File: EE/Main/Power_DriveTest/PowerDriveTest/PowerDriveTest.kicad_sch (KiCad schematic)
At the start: 46 parts, among them J1 Conn_01x02_Male, J2 Conn_01x03_Pin, J4 Conn_01x03_Pin, J5 Conn_01x03_Pin, P1 USB_C_Plug_USB2.0, Q1 Q_PMOS_GSD, Q2 Q_NMOS_GSD, SW1 SW_SPST, U1 LM3670MF-3.3, U4 MCP73832-2-OT

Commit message: Routine Checkout
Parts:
- removed R7: 0, Resistor_SMD:R_0402_1005Metric, symbol Device:R
- removed SW1: SW_SPST, Button_Switch_SMD:SW_Tactile_SPST_NO_Straight_CK_PTS636Sx25SMTRLFS, symbol Switch:SW_SPST
- added SW2: SW_DPST, symbol Switch:SW_DPST
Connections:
- net +3V3: now also SW2.1
- net GATE_EN: now also SW2.3
- net at R9.1: now also SW2.4
- new net BTN_SNS: SW2.2
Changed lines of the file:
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@@
 	)
 	(junction
-		(at 104.14 69.85)
-		(diameter 0)
-		(color 0 0 0 0)
-	)
-	(junction
 		(at 271.78 83.82)
 		(diameter 0)
@@
 	)
 	(junction
-		(at 118.11 69.85)
-		(diameter 0)
-		(color 0 0 0 0)
-	)
-	(junction
 		(at 233.68 130.81)
 		(diameter 0)
@@
 	(wire
 		(pts
-			(xy 104.14 69.85) (xy 104.14 73.66)
-		)
-		(stroke
-			(width 0)
-			(type default)
-		)
-	)
-	(wire
-		(pts
 			(xy 242.57 73.66) (xy 242.57 76.2)
 		)
@@
 	(wire
 		(pts
-			(xy 95.25 69.85) (xy 104.14 69.85)
+			(xy 95.25 69.85) (xy 106.68 69.85)
 		)
 		(stroke
@@
 	(wire
 		(pts
-			(xy 271.78 97.79) (xy 271.78 95.25)
+			(xy 116.84 69.85) (xy 123.19 69.85)
 		)
 		(stroke
@@
 	(wire
 		(pts
-			(xy 90.932 109.22) (xy 86.36 109.22)
+			(xy 271.78 97.79) (xy 271.78 95.25)
 		)
 		(stroke
@@
 	(wire
 		(pts
-			(xy 256.286 137.414) (xy 254.254 137.414)
+			(xy 90.932 109.22) (xy 86.36 109.22)
 		)
 		(stroke
@@
 	(wire
 		(pts
-			(xy 146.05 67.31) (xy 146.05 53.34)
+			(xy 256.286 137.414) (xy 254.254 137.414)
 		)
 		(stroke
@@
 	(wire
 		(pts
-			(xy 118.11 66.04) (xy 118.11 69.85)
+			(xy 146.05 67.31) (xy 146.05 53.34)
 		)
 		(stroke
@@
 	(wire
 		(pts
-			(xy 118.11 73.66) (xy 113.03 73.66)
-		)
-		(stroke
-			(width 0)
-			(type default)
-		)
-	)
-	(wire
-		(pts
 			(xy 85.09 55.88) (xy 85.09 69.85)
 		)
@@
 	(wire
 		(pts
-			(xy 118.11 69.85) (xy 123.19 69.85)
-		)
-		(stroke
-			(width 0)
-			(type default)
-		)
-	)
-	(wire
-		(pts
 			(xy 123.19 69.85) (xy 123.19 73.66)
 		)
@@
 	(wire
 		(pts
-			(xy 104.14 73.66) (xy 105.41 73.66)
-		)
-		(stroke
-			(width 0)
-			(type default)
-		)
-	)
-	(wire
-		(pts
 			(xy 250.19 90.17) (xy 251.46 90.17)
 		)
@@
 	(wire
 		(pts
-			(xy 104.14 66.04) (xy 104.14 69.85)
-		)
-		(stroke
-			(width 0)
-			(type default)
-		)
-	)
-	(wire
-		(pts
 			(xy 256.286 135.89) (xy 256.286 137.414)
 		)
@@
 	(wire
 		(pts
-			(xy 118.11 69.85) (xy 118.11 73.66)
-		)
-		(stroke
-			(width 0)
-			(type default)
-		)
-	)
-	(wire
-		(pts
 			(xy 252.73 83.82) (xy 255.27 83.82)
 		)
@@
 		)
 	)
-	(wire
-		(pts
-			(xy 114.3 66.04) (xy 118.11 66.04)
-		)
-		(stroke
-			(width 0)
-			(type default)
-		)
-	)
 	(text "Simulate GPIO toggles"
 		(exclude_from_sim no)
@@
 		)
 	)
+	(label "BTN_SNS"
+		(at 116.84 74.93 270)
+		(fields_autoplaced yes)
+		(effects
+			(font
+				(size 1.27 1.27)
+			)
+			(justify right bottom)
+		)
+	)
 	(symbol
 		(lib_id "Device:R")
@@
 	)
 	(symbol
+		(lib_id "Switch:SW_DPST")
+		(at 111.76 72.39 0)
+		(unit 1)
+		(exclude_from_sim no)
+		(in_bom yes)
+		(on_board yes)
+		(dnp no)
+		(fields_autoplaced yes)
+		(property "Reference" "SW2"
+			(at 111.76 63.9275 0)
+			(effects
+				(font
+					(size 1.27 1.27)
+				)
+			)
+		)
+		(property "Value" "SW_DPST"
+			(at 111.76 66.3518 0)
+			(effects
+				(font
+					(size 1.27 1.27)
+				)
+			)
+		)
+		(property "Footprint" ""
+			(at 111.76 72.39 0)
+			(effects
+				(font
+					(size 1.27 1.27)
+				)
+				(hide yes)
+			)
+		)
+		(property "Datasheet" "~"
+			(at 111.76 72.39 0)
+			(effects
+				(font
+					(size 1.27 1.27)
+				)
+				(hide yes)
+			)
+		)
+		(property "Description" "Double Pole Single Throw (DPST) Switch"
+			(at 111.76 72.39 0)
+			(effects
+				(font
+					(size 1.27 1.27)
+				)
+				(hide yes)
+			)
+		)
+		(pin "4"
+		)
+		(pin "3"
+		)
+		(pin "1"
+		)
+		(pin "2"
+		)
+		(instances
+			(project ""
+				(path "/42daf986-15ca-4106-89ad-61486dd904de"
+					(reference "SW2")
+					(unit 1)
+				)
+			)
+		)
+	)
+	(symbol
 		(lib_id "Device:C")
 		(at 254.254 143.002 0)
@@
 	)
 	(symbol
-		(lib_id "Device:R")
-		(at 109.22 73.66 90)
-		(unit 1)
-		(exclude_from_sim no)
-		(in_bom yes)
-		(on_board yes)
-		(dnp no)
-		(property "Reference" "R7"
-			(at 109.22 71.374 90)
-			(effects
-				(font
-					(size 1.27 1.27)
-				)
-			)
-		)
-		(property "Value" "0"
-			(at 109.22 73.66 90)
-			(effects
-				(font
-					(size 1.27 1.27)
-				)
-			)
-		)
-		(property "Footprint" "Resistor_SMD:R_0402_1005Metric"
-			(at 109.22 75.438 90)
-			(effects
-				(font
-					(size 1.27 1.27)
-				)
-				(hide yes)
-			)
-		)
-		(property "Datasheet" "~"
-			(at 109.22 73.66 0)
-			(effects
-				(font
-					(size 1.27 1.27)
-				)
-				(hide yes)
-			)
-		)
-		(property "Description" "Resistor"
-			(at 109.22 73.66 0)
-			(effects
-				(font
-					(size 1.27 1.27)
-				)
-				(hide yes)
-			)
-		)
-		(pin "1"
-		)
-		(pin "2"
-		)
-		(instances
-			(project "PowerDriveTest"
-				(path "/42daf986-15ca-4106-89ad-61486dd904de"
-					(reference "R7")
-					(unit 1)
-				)
-			)
-		)
-	)
-	(symbol
 		(lib_name "GND_1")
 		(lib_id "power:GND")
@@
 	)
 	(symbol
+		(lib_id "power:+3V3")
+		(at 106.68 74.93 90)
+		(unit 1)
+		(exclude_from_sim no)
+		(in_bom yes)
+		(on_board yes)
+		(dnp no)
+		(fields_autoplaced yes)
+		(property "Reference" "#PWR029"
+			(at 110.49 74.93 0)
+			(effects
+				(font
+					(size 1.27 1.27)
+				)
+				(hide yes)
+			)
+		)
+		(property "Value" "+3V3"
+			(at 103.505 74.93 90)
+			(effects
+				(font
+					(size 1.27 1.27)
+				)
+				(justify left)
+			)
+		)
+		(property "Footprint" ""
+			(at 106.68 74.93 0)
+			(effects
+				(font
+					(size 1.27 1.27)
+				)
+				(hide yes)
+			)
+		)
+		(property "Datasheet" ""
+			(at 106.68 74.93 0)
+			(effects
+				(font
+					(size 1.27 1.27)
+				)
+				(hide yes)
+			)
+		)
+		(property "Description" "Power symbol creates a global label with name \"+3V3\""
+			(at 106.68 74.93 0)
+			(effects
+				(font
+					(size 1.27 1.27)
+				)
+				(hide yes)
+			)
+		)
+		(pin "1"
+		)
+		(instances
+			(project "PowerDriveTest"
+				(path "/42daf986-15ca-4106-89ad-61486dd904de"
+					(reference "#PWR029")
+					(unit 1)
+				)
+			)
+		)
+	)
+	(symbol
 		(lib_id "Device:R")
 		(at 143.51 71.12 0)
@@
 					(unit 1)
 				)
-			)
-		)
-	)
-	(symbol
-		(lib_id "Switch:SW_SPST")
-		(at 109.22 66.04 0)
-		(unit 1)
-		(exclude_from_sim no)
-		(in_bom yes)
-		(on_board yes)
-		(dnp no)
-		(fields_autoplaced yes)
-		(property "Reference" "SW1"
-			(at 109.22 60.2445 0)
-			(effects
-				(font
-					(size 1.27 1.27)
-				)
-			)
-		)
-		(property "Value" "SW_SPST"
-			(at 109.22 62.6688 0)
-			(effects
-				(font
-					(size 1.27 1.27)
-				)
-			)
-		)
-		(property "Footprint" "Button_Switch_SMD:SW_Tactile_SPST_NO_Straight_CK_PTS636Sx25SMTRLFS"
-			(at 109.22 66.04 0)
-			(effects
-				(font
-					(size 1.27 1.27)
-				)
-				(hide yes)
-			)
-		)
-		(property "Datasheet" "~"
-			(at 109.22 66.04 0)
-			(effects
-				(font
-					(size 1.27 1.27)
-				)
-				(hide yes)
-			)
-		)
-		(property "Description" "Single Pole Single Throw (SPST) switch"
-			(at 109.22 66.04 0)
-			(effects
-				(font
-					(size 1.27 1.27)
-				)
-				(hide yes)
-			)
-		)
-		(pin "2"
-		)
-		(pin "1"
-		)
-		(instances
-			(project "PowerDriveTest"
-				(path "/42daf986-15ca-4106-89ad-61486dd904de"
-					(reference "SW1")
-					(unit 1)
-				)

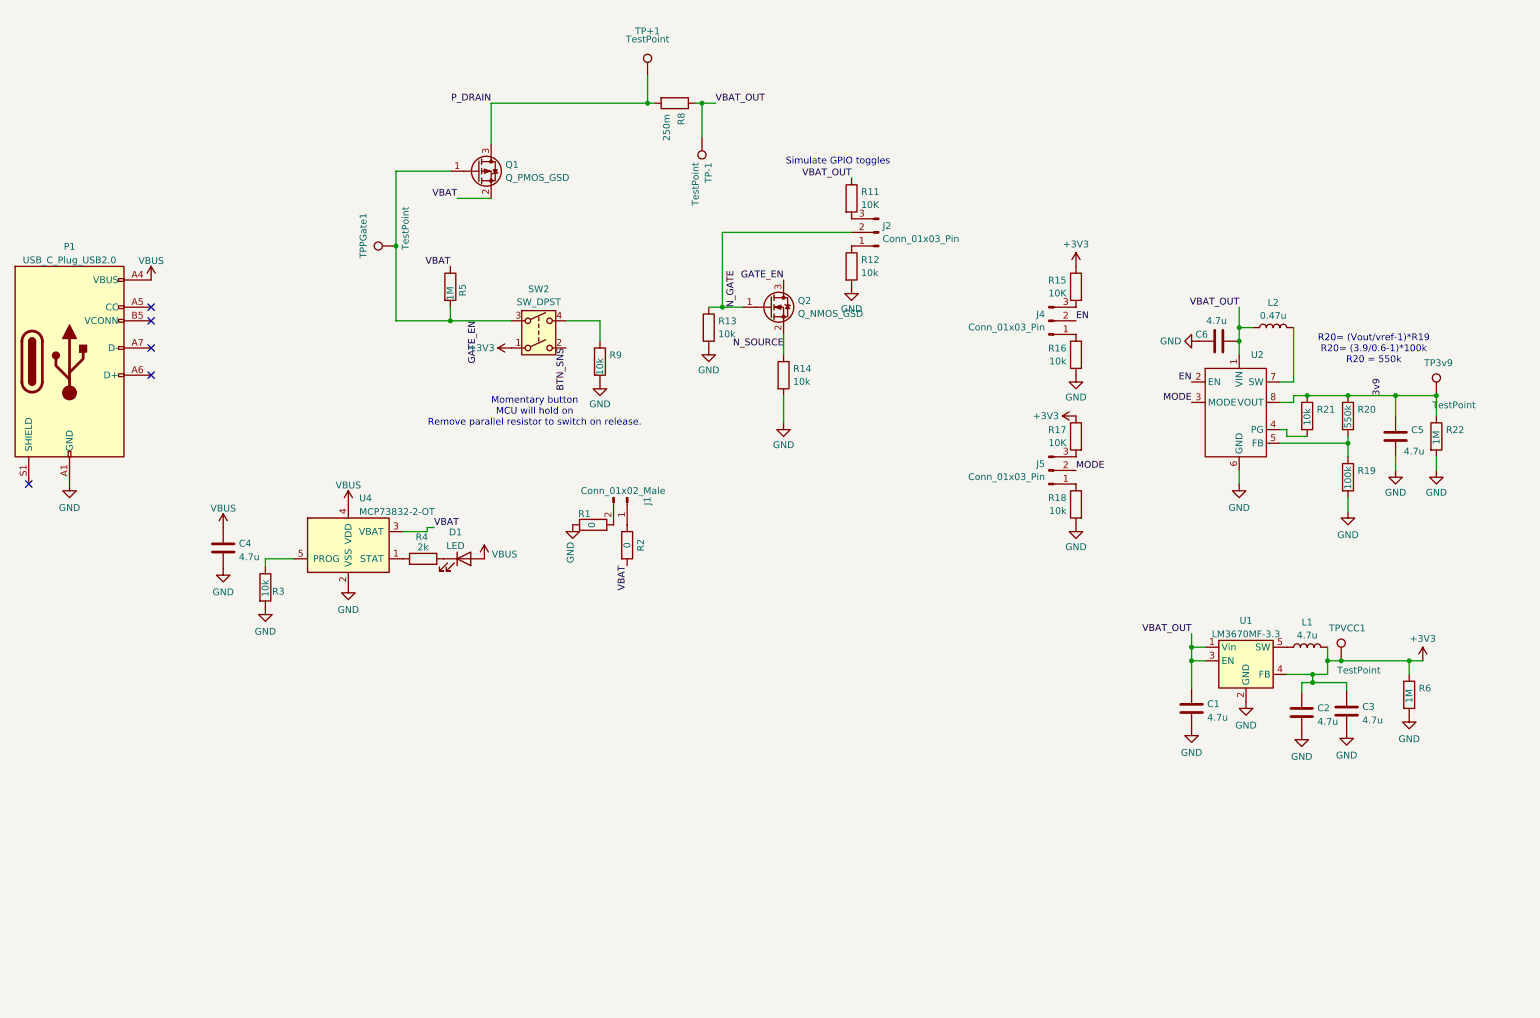
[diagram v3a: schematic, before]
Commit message: Schematic Change, Attempting new power circuit to turn off, with MCU
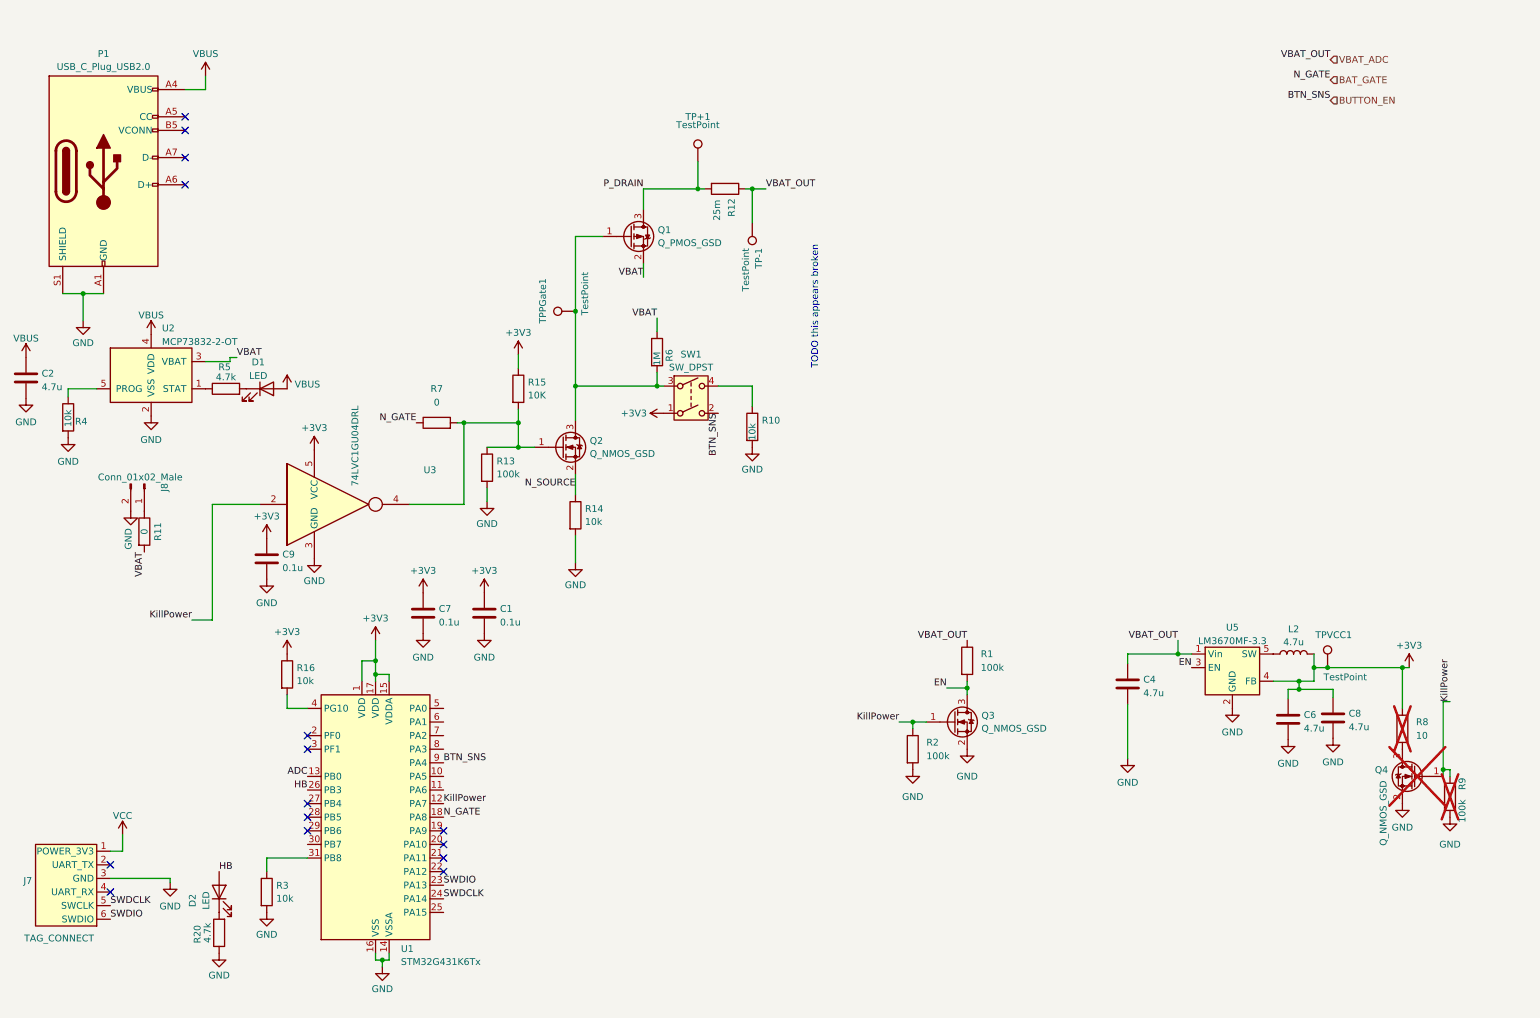
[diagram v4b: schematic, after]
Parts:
- removed C3, C5: 4.7u, Capacitor_SMD:C_0603_1608Metric, symbol Device:C
- removed J1: Conn_01x02_Male, Connector_JST:JST_PH_B2B-PH-K_1x02_P2.00mm_Vertical, symbol Connector:Conn_01x02_Male
- removed J2, J4, J5: Conn_01x03_Pin, Connector_PinHeader_2.54mm:PinHeader_1x03_P2.54mm_Vertical, symbol Connector:Conn_01x03_Pin
- removed L1: 4.7u, Inductor_SMD:L_0805_2012Metric, symbol Device:L
- removed R17: 10K, Resistor_SMD:R_0402_1005Metric, symbol Device:R
- removed R18, R21: 10k, Resistor_SMD:R_0402_1005Metric, symbol Device:R
- removed R19: 100k, Resistor_SMD:R_0402_1005Metric, symbol Device:R
- removed R22: 1M, Resistor_SMD:R_0402_1005Metric, symbol Device:R
- removed SW2: SW_DPST, symbol Switch:SW_DPST
- removed TP3v9: TestPoint, TestPoint:TestPoint_Pad_1.5x1.5mm, symbol Connector:TestPoint
- removed U1: LM3670MF-3.3, Package_TO_SOT_SMD:TSOT-23-5, symbol Regulator_Switching:LM3670MF
- removed U2: ~, Package_TO_SOT_SMD:SOT-583-8, symbol library:TPS61033
- removed U4: MCP73832-2-OT, Package_TO_SOT_SMD:SOT-23-5, symbol Battery_Management:MCP73832-2-OT
- added C7, C9: 0.1u, Capacitor_SMD:C_0402_1005Metric, symbol Device:C
- added C8: 4.7u, Capacitor_SMD:C_0603_1608Metric, symbol Device:C
- added D2: LED, LED_SMD:LED_0603_1608Metric, symbol Device:LED
- added J7: TAG_CONNECT, Connector:Tag-Connect_TC2030-IDC-FP_2x03_P1.27mm_Vertical, symbol ACTempDisconnect:TAG_CONNECT
- added J8: Conn_01x02_Male, Connector_JST:JST_PH_B2B-PH-K_1x02_P2.00mm_Vertical, symbol Connector:Conn_01x02_Male
- added Q3, Q4: Q_NMOS_GSD, Package_TO_SOT_SMD:SOT-23, symbol Device:Q_NMOS_GSD
- added R10: 10k, Resistor_SMD:R_0402_1005Metric_Pad0.72x0.64mm_HandSolder, symbol Device:R
- added R7: 0, Resistor_SMD:R_0402_1005Metric_Pad0.72x0.64mm_HandSolder, symbol Device:R
- added SW1: SW_DPST, Library:401-1133-ND, symbol Switch:SW_DPST
- added U1: STM32G431K6Tx, Package_QFP:LQFP-32_7x7mm_P0.8mm, symbol MCU_ST_STM32G4:STM32G431K6Tx
- added U2: MCP73832-2-OT, Package_TO_SOT_SMD:SOT-23-5, symbol Battery_Management:MCP73832-2-OT
- added U3: 74LVC1GU04DRL, Package_TO_SOT_SMD:SOT-553, symbol 74xGxx:74LVC1GU04DRL
- added U5: LM3670MF-3.3, Package_TO_SOT_SMD:TSOT-23-5, symbol Regulator_Switching:LM3670MF
- C1: value 4.7u -> 0.1u; footprint Capacitor_SMD:C_0603_1608Metric -> Capacitor_SMD:C_0402_1005Metric
- L2: value 0.47u -> 4.7u; P/N (none) -> 74479775222A
- R1, R2: value 0 -> 100k; footprint Resistor_SMD:R_0402_1005Metric -> Resistor_SMD:R_0402_1005Metric_Pad0.72x0.64mm_HandSolder
- R11: value 10K -> 0; footprint Resistor_SMD:R_0402_1005Metric -> Resistor_SMD:R_0402_1005Metric_Pad0.72x0.64mm_HandSolder
- R12: value 10k -> 25m; footprint Resistor_SMD:R_0402_1005Metric -> Resistor_SMD:R_0805_2012Metric_Pad1.20x1.40mm_HandSolder
- R13: value 10k -> 100k; footprint Resistor_SMD:R_0402_1005Metric -> Resistor_SMD:R_0402_1005Metric_Pad0.72x0.64mm_HandSolder
- R14, R15, R16, R3, R6: footprint Resistor_SMD:R_0402_1005Metric -> Resistor_SMD:R_0402_1005Metric_Pad0.72x0.64mm_HandSolder
- R20: value 550k -> 4.7k; footprint Resistor_SMD:R_0402_1005Metric -> Resistor_SMD:R_0402_1005Metric_Pad0.72x0.64mm_HandSolder
- R4: value 2k -> 10k; footprint Resistor_SMD:R_0402_1005Metric -> Resistor_SMD:R_0402_1005Metric_Pad0.72x0.64mm_HandSolder
- R5: value 1M -> 4.7k; footprint Resistor_SMD:R_0402_1005Metric -> Resistor_SMD:R_0402_1005Metric_Pad0.72x0.64mm_HandSolder
- R8: value 250m -> 10; footprint Resistor_SMD:R_0805_2012Metric -> Resistor_SMD:R_0402_1005Metric_Pad0.72x0.64mm_HandSolder; now not fitted
- R9: value 10k -> 100k; footprint Resistor_SMD:R_0402_1005Metric -> Resistor_SMD:R_0402_1005Metric_Pad0.72x0.64mm_HandSolder; now not fitted
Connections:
- net 3v9 is gone; now on net GND: R20.1
- net N_GATE is gone; now on an unnamed net: Q2.1 (G), R13.1
- net +3V3: now also C1.1, C6.1, L2.2, R16.1, R8.1, C7.1, C8.1, C9.1, SW1.1, U1.1 (VDD), U1.15 (VDDA), U1.17 (VDD), U3.5 (VCC), U5.4 (FB); no longer C2.1, R6.1
- net EN: now also R1.2, Q3.3 (D), U5.3 (EN)
- net GND: now also C6.2, P1.S1 (SHIELD), R2.2, R4.2, C7.2, C8.2, C9.2, J7.3 (GND), J8.2 (Pin_2), Q3.2 (S), Q4.2 (S), R10.2, U1.14 (VSSA), U1.16 (VSS), U1.32 (VSS), U2.2 (VSS), U3.3 (GND), U5.2 (GND); no longer C6.1, R1.1, R12.2, R16.2, R6.2
- net P_DRAIN: now also R12.2; no longer R8.2
- net VBAT: now also R11.2, R6.1, U2.3 (VBAT); no longer R2.2, R5.1
- net VBUS: now also C2.1, U2.4 (VDD); no longer C4.1
- net at R4.1: now also U2.5 (PROG)
- net at R3.1: now also U1.31 (PB8)
- net KillPower: now reaches R9.1
- net KillPower: now also R2.1, Q3.1 (G), Q4.1 (G), U1.12 (PA7), U3.2
- net VBAT_ADC: now reaches R12.1
- net VBAT_ADC: now also C4.1, R1.1, TP-1.1, U5.1 (Vin)
- net at R15.2: now also R7.2, U3.4
- net at R20.2: now also D2.1 (K)
- net at D1.1 (K): now also R5.2; no longer R4.2
- net GATE_EN: no longer names the net of Q1.1 (G), Q2.3 (D), TPPGate1.1
- net GATE_EN: now also R6.2, SW1.3; no longer R5.2
- removed net VBAT_OUT: C1.1, C6.2, L2.1, R11.1, R8.1, TP-1.1
- new net: J8.1 (Pin_1), R11.1
- new net: L2.1, U5.5 (SW)
- new net: Q4.3 (D), R8.2
- new net: R16.2, U1.4 (PG10)
- new net: R10.1, SW1.4
- new net: R5.1, U2.1 (STAT)
- new net ADC: U1.13 (PB0)
- new net BAT_GATE: R7.1, U1.18 (PA8)
- new net BUTTON_EN: SW1.2, U1.9 (PA4)
- new net HB: D2.2 (A), U1.26 (PB3)
- new net SWDCLK: J7.5 (SWCLK), U1.24 (PA14)
- new net SWDIO: J7.6 (SWDIO), U1.23 (PA13)
- new net VCC: J7.1 (POWER_3V3)
- no-connect marks 5 -> 15
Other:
- note added: "TODO this appears broken"
- note removed: "Momentary button MCU will hold on Remove parallel resistor to switch on release."
- note removed: "R20= (Vout/vref-1)*R19 R20= (3.9/0.6-1)*100k R20 = 550k"
- note removed: "Simulate GPIO toggles"

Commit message: Adding Test Circuit 2
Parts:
- added KP1, NGATE1: TestPoint, TestPoint:TestPoint_Pad_1.5x1.5mm, symbol Connector:TestPoint
- R8: footprint Resistor_SMD:R_0402_1005Metric_Pad0.72x0.64mm_HandSolder -> Resistor_SMD:R_0805_2012Metric_Pad1.20x1.40mm_HandSolder
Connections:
- net VCC is gone; now on net +3V3: J7.1 (POWER_3V3)
- net BAT_GATE: now also U1.10 (PA5); no longer U1.18 (PA8)
- net HB: now also U1.22 (PA12); no longer U1.26 (PB3)
- net KillPower: now also U1.8 (PA3), KP1.1; no longer U1.12 (PA7)
- net at Q2.1 (G), R13.1, R15.2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: now also NGATE1.1
- no-connect marks 15 -> 16
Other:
- note removed: "TODO this appears broken"
